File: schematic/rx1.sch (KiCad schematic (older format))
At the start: 34 parts, among them Q14 2N3904, Q15 2N3904, SW11 SW_SPDT, T3 FT37-43, T4 FT37-43, U9 ADE-1

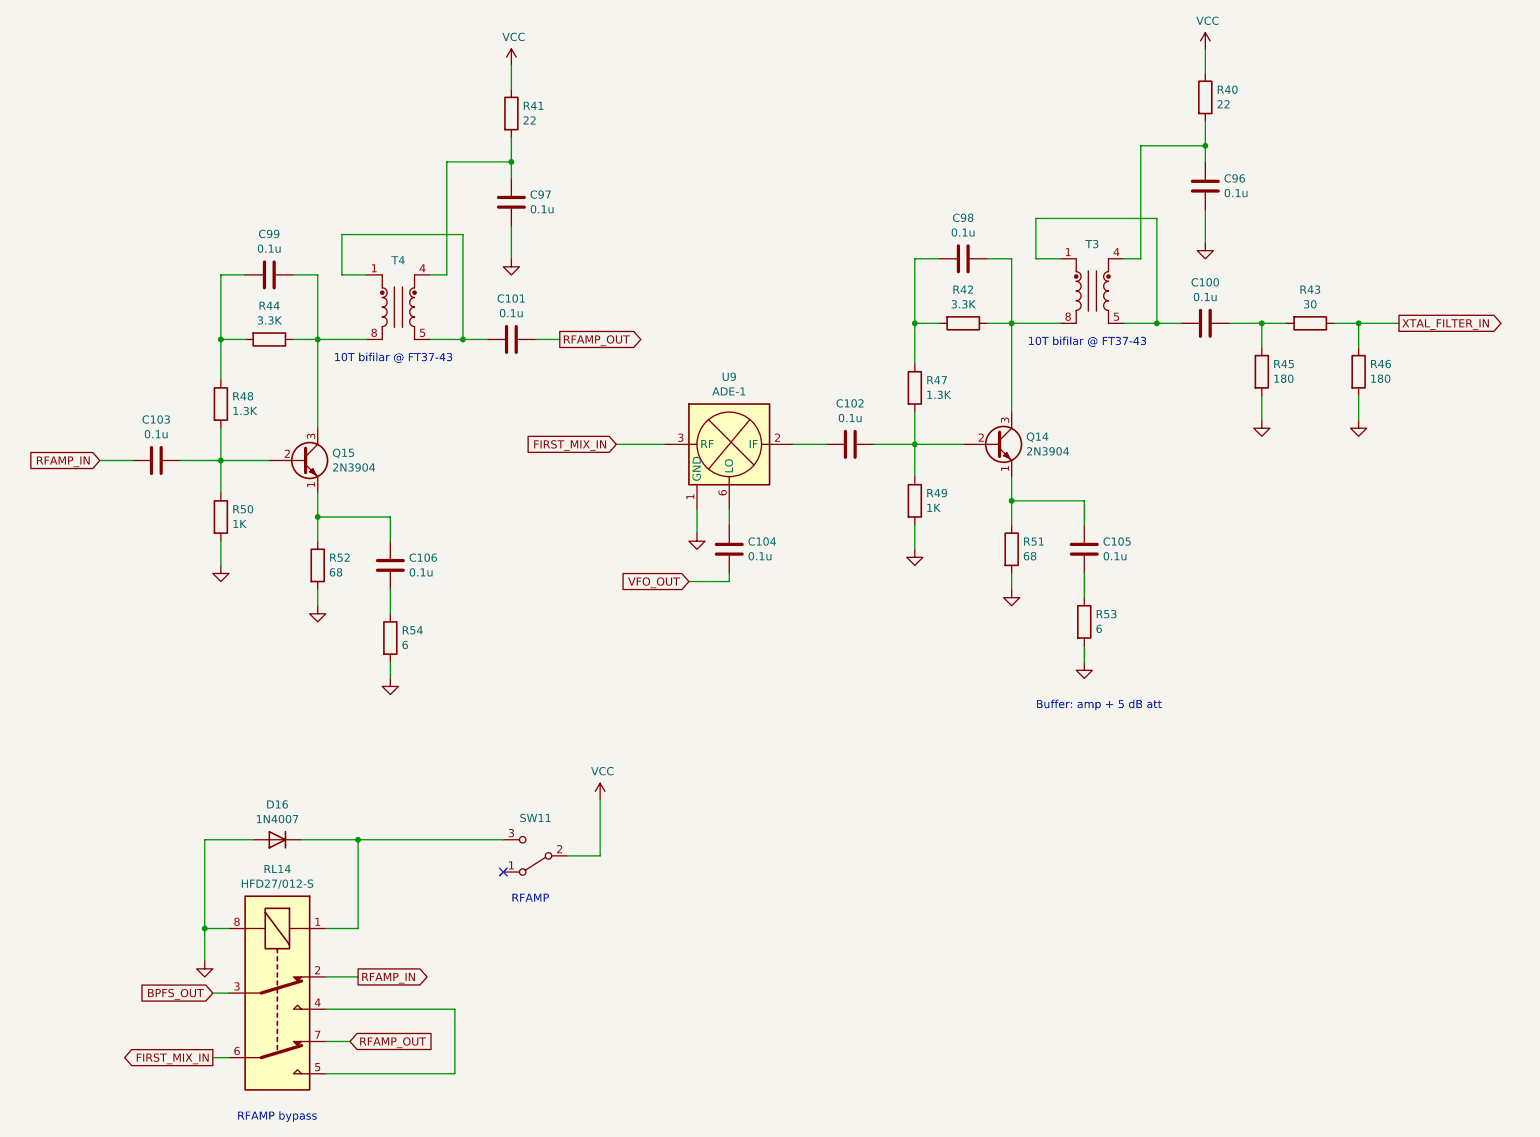
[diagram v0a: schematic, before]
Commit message: Correct the schematic
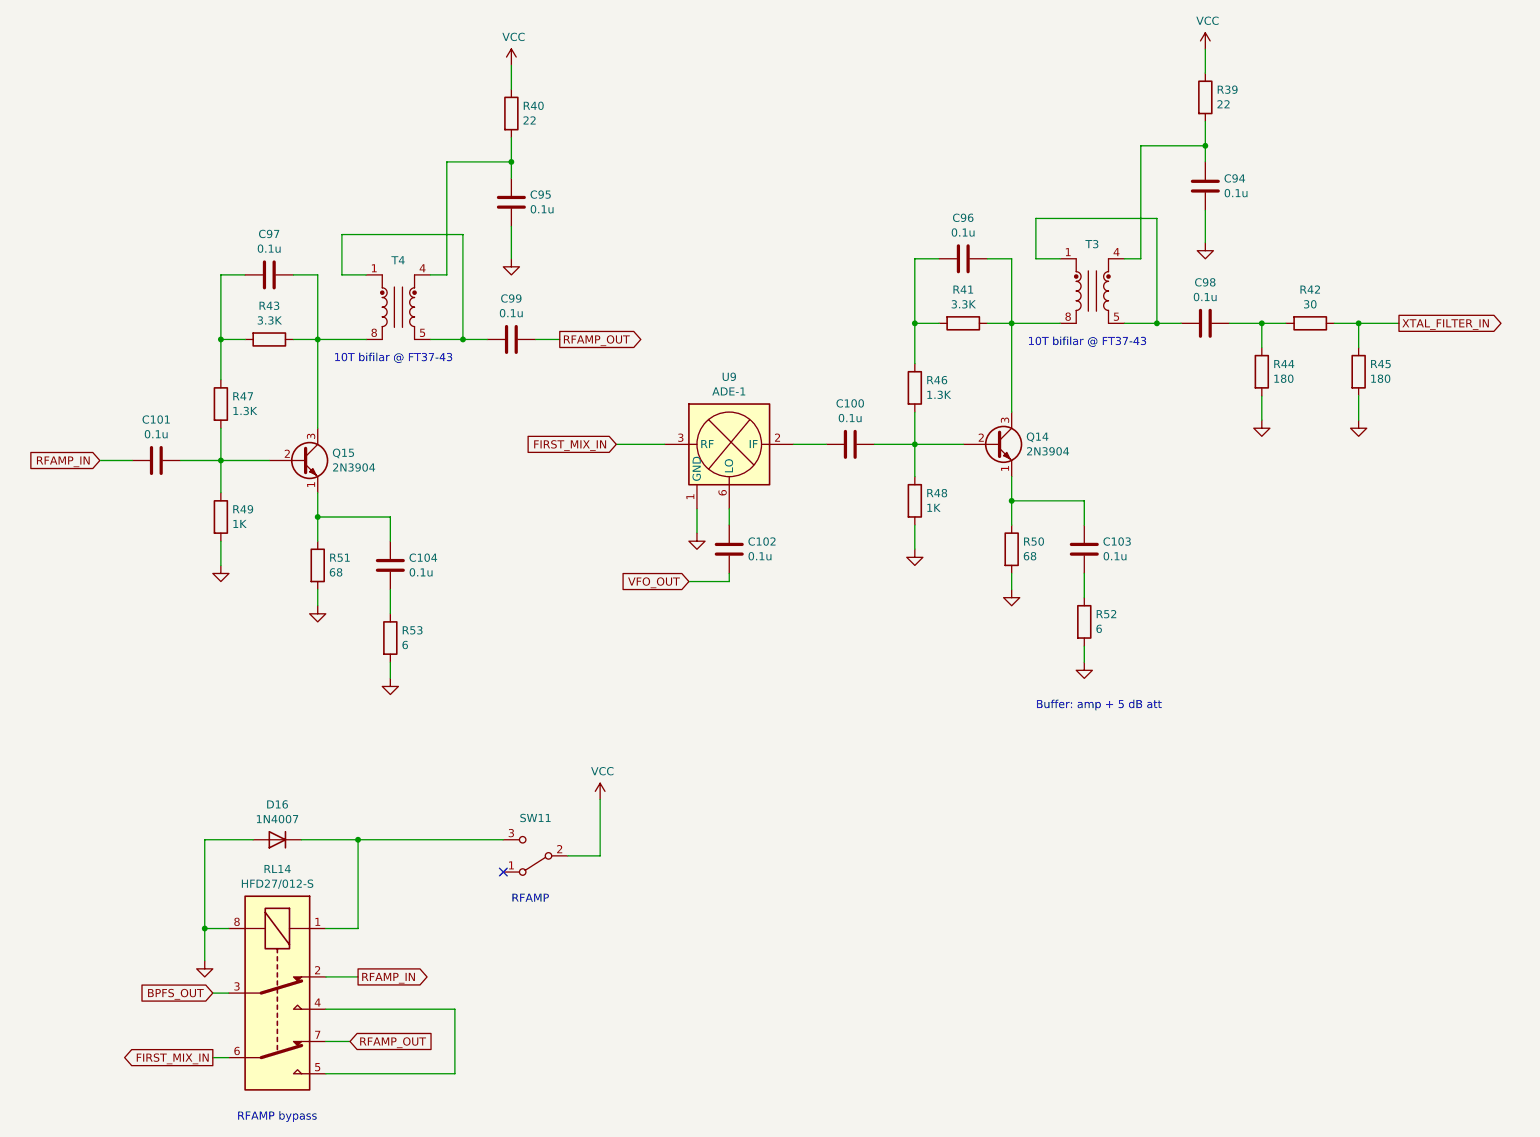
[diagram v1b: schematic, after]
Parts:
- renumbered C102 to C100, C103 to C101, C104 to C102, C105 to C103, C106 to C104, C96 to C94, C97 to C95, C98 to C96, C99 to C97, C100 to C98, C101 to C99, R40 to R39, R41 to R40, R42 to R41, R43 to R42, R44 to R43, R45 to R44, R46 to R45, R47 to R46, R48 to R47, R49 to R48, R50 to R49, R51 to R50, R52 to R51, R53 to R52, R54 to R53
